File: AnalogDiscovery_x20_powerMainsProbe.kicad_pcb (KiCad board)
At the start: 2 copper layers, 64 x 64 mm, 22 parts, among them J1 Conn_02x15_Counter_Clockwise, J2 Conn_01x03_Female, J3 Conn_01x03_Female, J4 Conn_01x03_Male, J5 Conn_01x03_Male, J6 Conn_02x03_Counter_Clockwise

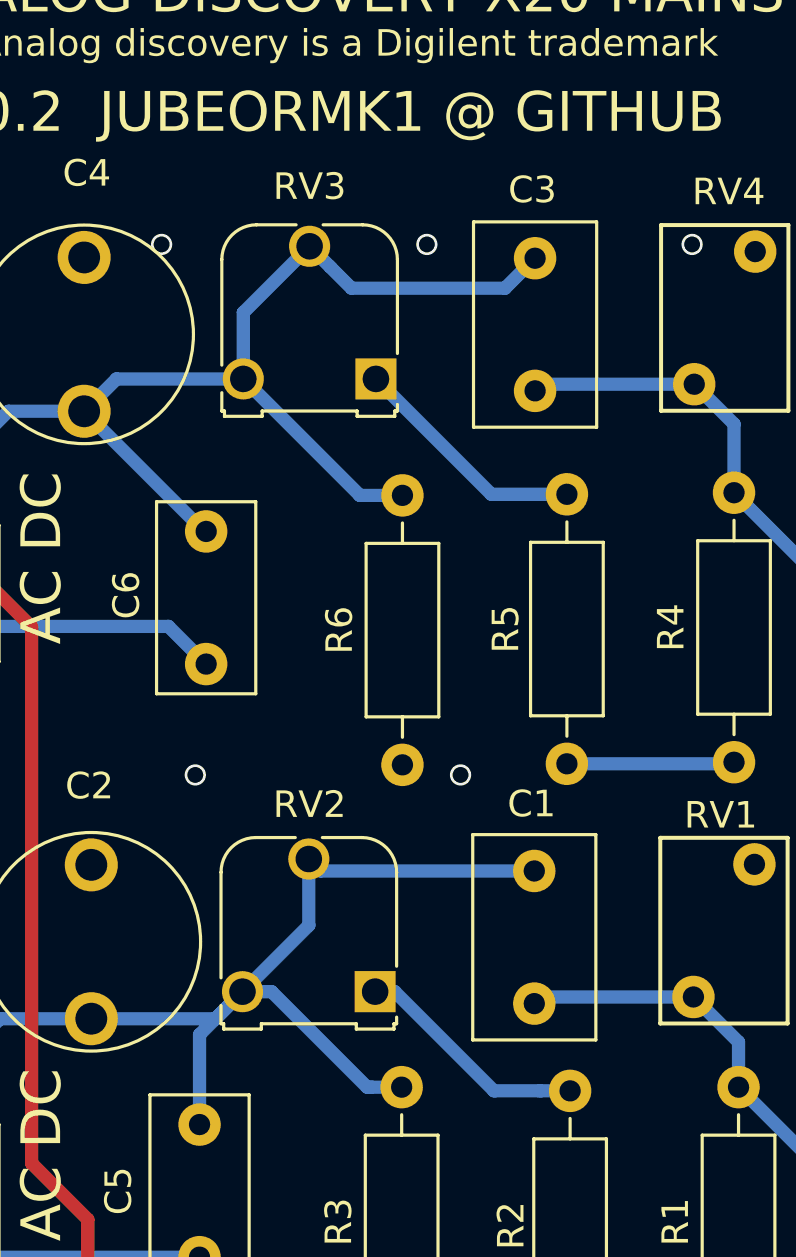
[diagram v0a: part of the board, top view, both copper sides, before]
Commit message: Footprint fixed for potentiometers
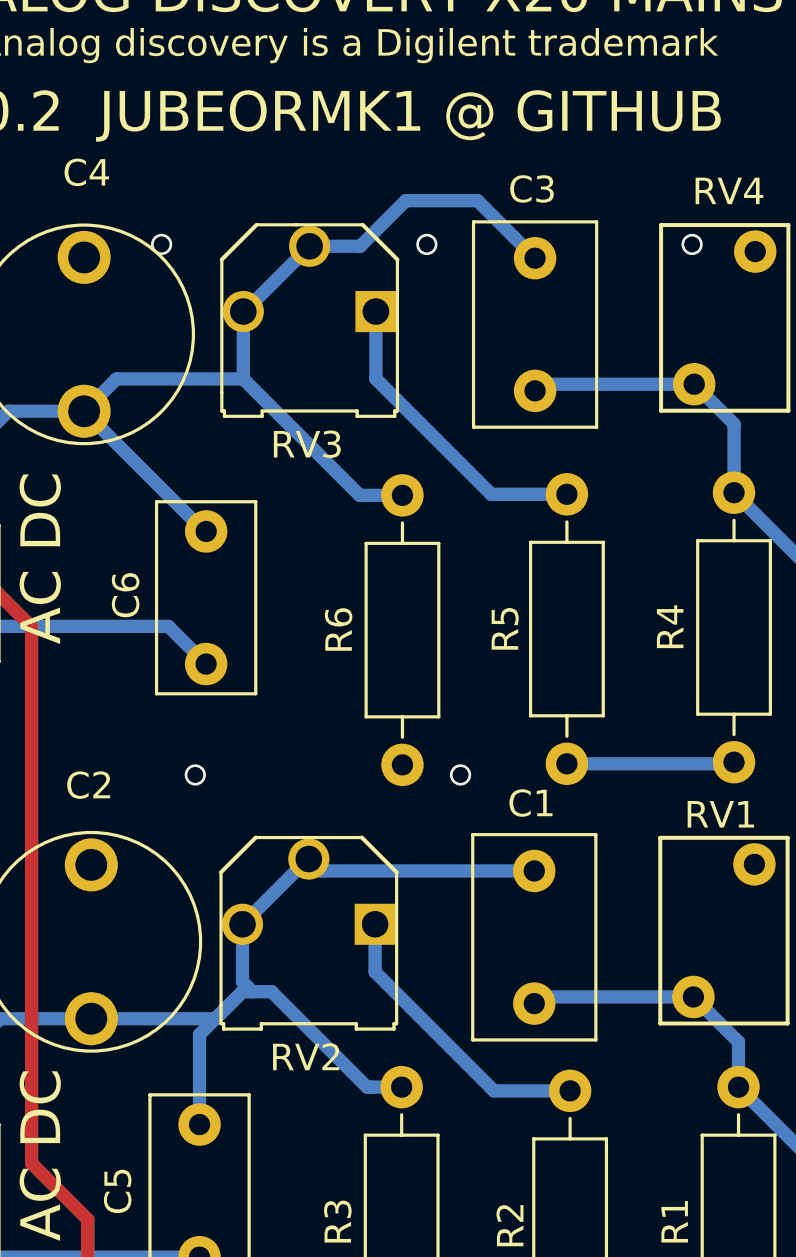
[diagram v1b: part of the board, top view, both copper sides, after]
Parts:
- RV2, RV3: footprint Potentiometer_THT:Potentiometer_Runtron_RM-065_Vertical -> my_footprint_library:Potentiometer_Bourns_3306P-1-504
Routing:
- net Net-(R2-Pad1): track 8.90 -> 11.0 mm
- net Net-(R5-Pad1): track 9.00 -> 10.9 mm
